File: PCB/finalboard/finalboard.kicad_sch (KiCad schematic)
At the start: 1 part, among them U1 ESP32-S3-WROOM-1

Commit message: FinalBoard Changes
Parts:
- added J1: USB_C_Receptacle_USB2.0, symbol Connector:USB_C_Receptacle_USB2.0
- added J2, J3: Conn_01x04, symbol Connector_Generic:Conn_01x04
- added R1, R2: 5k, symbol Device:R
- added U2: ~, symbol wc_sys_symbol:LCD3.5
- added U3: USBLC6-2SC6, Package_TO_SOT_SMD:SOT-23-6, symbol Power_Protection:USBLC6-2SC6
- added U4: ~, symbol wc_sys_symbol:GPS
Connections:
- net ESP_TX1: now reaches U1.10 (GPIO17/U1TXD/ADC2_CH6)
- net ESP_RX1: now reaches U1.11 (GPIO18/U1RXD/ADC2_CH7/CLK_OUT3)
- net USB_D-: now reaches U1.13 (GPIO19/U1RTS/ADC2_CH8/CLK_OUT2/USB_D-)
- net USB_D-: now also U3.3 (I/O2)
- net USB_D+: now reaches U1.14 (GPIO20/U1CTS/ADC2_CH9/CLK_OUT1/USB_D+)
- net USB_D+: now also U3.1 (I/O1)
- net ESP_RX0: now reaches U1.36 (U0RXD/GPIO44/CLK_OUT2)
- net ESP_TX0: now reaches U1.37 (U0TXD/GPIO43/CLK_OUT1)
- new net: J1.A5 (CC1), R2.1
- new net: J1.A4 (VBUS), J1.A9 (VBUS), J1.B4 (VBUS), J1.B9 (VBUS), U3.5 (VBUS)
- new net: J1.A6 (D+), J1.B6 (D+)
- new net: J1.A7 (D-), J1.B7 (D-)
- new net: J1.B5 (CC2), R1.1
- new net GND: J1.A1 (GND), J1.A12 (GND), J1.B1 (GND), J1.B12 (GND), R1.2, R2.2, U3.2 (GND)
- no-connect marks 0 -> 3
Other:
- company: (none) -> USF IEEE Electrathon
- title: (none) -> Wireless Communication System
- moved on the sheet: U1

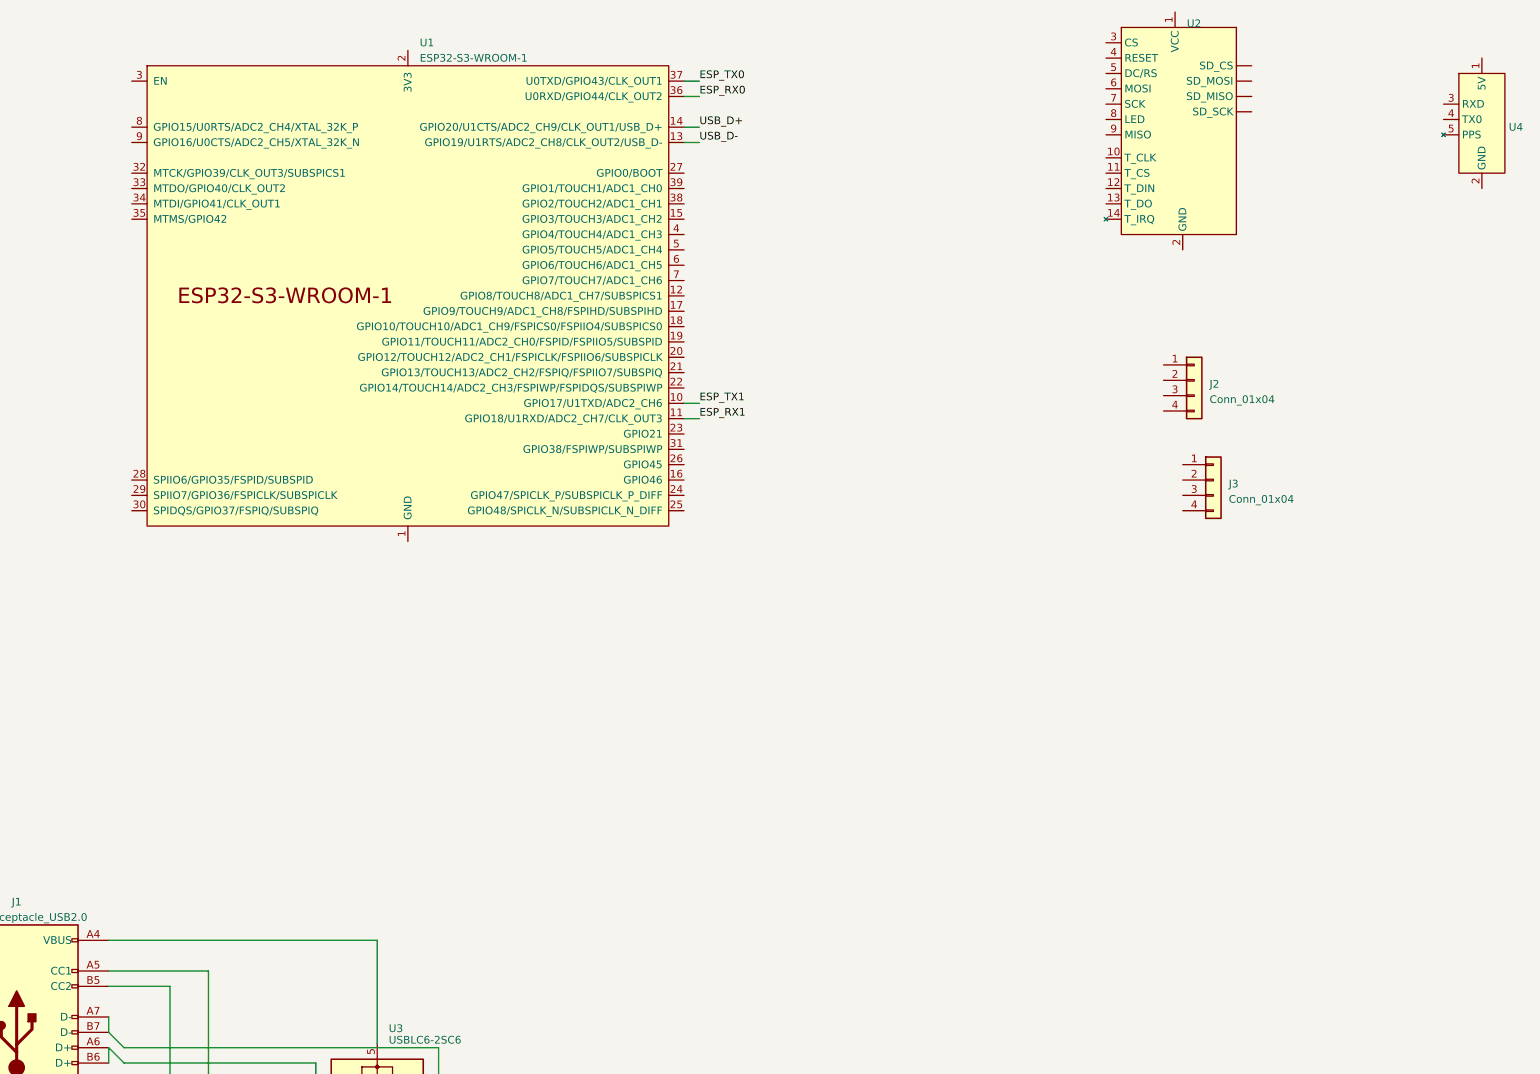
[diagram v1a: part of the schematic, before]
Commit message: Design Iterations
added touch buttons
wired SPI sdcard and display
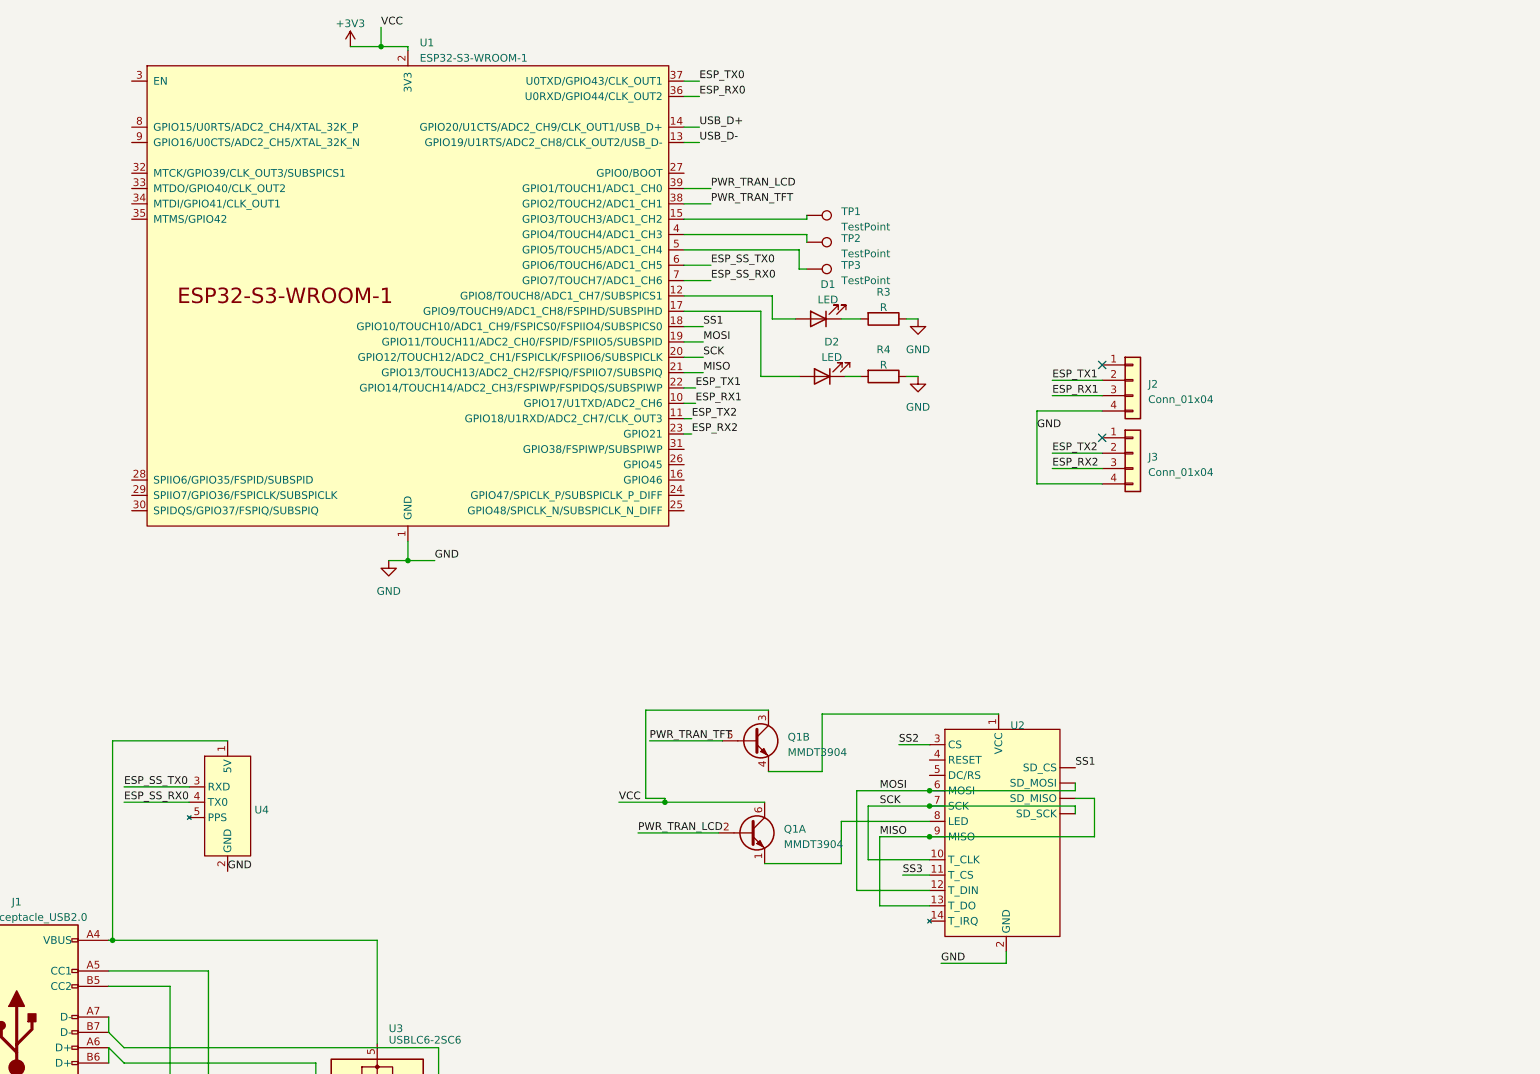
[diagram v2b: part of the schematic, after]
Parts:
- added D1, D2: LED, LED_SMD:LED_2512_6332Metric_Pad1.52x3.35mm_HandSolder, symbol Device:LED
- added Q1: MMDT3904, Package_TO_SOT_SMD:SOT-363_SC-70-6, symbol Transistor_BJT:MMDT3904
- added R3, R4: R, Resistor_SMD:R_1210_3225Metric_Pad1.30x2.65mm_HandSolder, symbol Device:R
- added TP1, TP2, TP3: TestPoint, TestPoint:TestPoint_Pad_D4.0mm, symbol Connector:TestPoint
- J1: footprint (none) -> Connector_USB:USB_C_Receptacle_Palconn_UTC16-G
- J2, J3: footprint (none) -> Connector_PinSocket_2.54mm:PinSocket_1x04_P2.54mm_Vertical_SMD_Pin1Left
- R1, R2: footprint (none) -> Resistor_SMD:R_1210_3225Metric_Pad1.30x2.65mm_HandSolder
- U2: footprint (none) -> wc_sys_footprint:LCD3.5tft
- U4: footprint (none) -> wc_sys_footprint:NEO-6M
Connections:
- net ESP_RX1: now also J2.3 (Pin_3), U1.10 (GPIO17/U1TXD/ADC2_CH6); no longer U1.11 (GPIO18/U1RXD/ADC2_CH7/CLK_OUT3)
- net ESP_TX1: now also J2.2 (Pin_2), U1.22 (GPIO14/TOUCH14/ADC2_CH3/FSPIWP/FSPIDQS/SUBSPIWP); no longer U1.10 (GPIO17/U1TXD/ADC2_CH6)
- net GND: now also J2.4 (Pin_4), J3.4 (Pin_4), U1.1 (GND), U1.40 (GND), U1.41 (GND), U2.2 (GND), U4.2 (GND), R3.1, R4.1
- net at U1.12 (GPIO8/TOUCH8/ADC1_CH7/SUBSPICS1): now also D1.2 (A)
- net at U1.15 (GPIO3/TOUCH3/ADC1_CH2): now also TP1.1
- net at U1.17 (GPIO9/TOUCH9/ADC1_CH8/FSPIHD/SUBSPIHD): now also D2.2 (A)
- net SS1: now reaches U1.18 (GPIO10/TOUCH10/ADC1_CH9/FSPICS0/FSPIIO4/SUBSPICS0)
- net SS1: now also U2. (SD_SCK)
- net MOSI: now reaches U1.19 (GPIO11/TOUCH11/ADC2_CH0/FSPID/FSPIIO5/SUBSPID)
- net MOSI: now also U2. (SD_SCK), U2.12 (T_DIN), U2.6 (MOSI)
- net +3V3: now reaches U1.2 (3V3)
- net +3V3: now also Q1.3 (C2), Q1.6 (C1)
- net SCK: now reaches U1.20 (GPIO12/TOUCH12/ADC2_CH1/FSPICLK/FSPIIO6/SUBSPICLK)
- net SCK: now also U2. (SD_SCK), U2.10 (T_CLK), U2.7 (SCK)
- net MISO: now reaches U1.21 (GPIO13/TOUCH13/ADC2_CH2/FSPIQ/FSPIIO7/SUBSPIQ)
- net MISO: now also U2. (SD_SCK), U2.13 (T_DO), U2.9 (MISO)
- net ESP_RX2: now reaches U1.23 (GPIO21)
- net ESP_RX2: now also J3.3 (Pin_3)
- net PWR_TRAN_TFT: now reaches U1.38 (GPIO2/TOUCH2/ADC1_CH1)
- net PWR_TRAN_TFT: now also Q1.5 (B2)
- net PWR_TRAN_LCD: now reaches U1.39 (GPIO1/TOUCH1/ADC1_CH0)
- net PWR_TRAN_LCD: now also Q1.2 (B1)
- net at U1.4 (GPIO4/TOUCH4/ADC1_CH3): now also TP2.1
- net at U1.5 (GPIO5/TOUCH5/ADC1_CH4): now also TP3.1
- net ESP_SS_TX0: now reaches U1.6 (GPIO6/TOUCH6/ADC1_CH5)
- net ESP_SS_TX0: now also U4.3 (RXD)
- net ESP_SS_RX0: now reaches U1.7 (GPIO7/TOUCH7/ADC1_CH6)
- net ESP_SS_RX0: now also U4.4 (TX0)
- net at U2.1 (VCC): now also Q1.4 (E2)
- net SS3: now reaches U2.11 (T_CS)
- net SS2: now reaches U2.3 (CS)
- net at U2.8 (LED): now also Q1.1 (E1)
- net at J1.A4 (VBUS), J1.A9 (VBUS), J1.B4 (VBUS)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: now also U4.1 (5V)
- net ESP_TX2: now reaches J3.2 (Pin_2)
- net ESP_TX2: now also U1.11 (GPIO18/U1RXD/ADC2_CH7/CLK_OUT3)
- new net: D1.1 (K), R3.2
- new net: D2.1 (K), R4.2
- no-connect marks 3 -> 5
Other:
- moved on the sheet: J2, J3, U2, U4

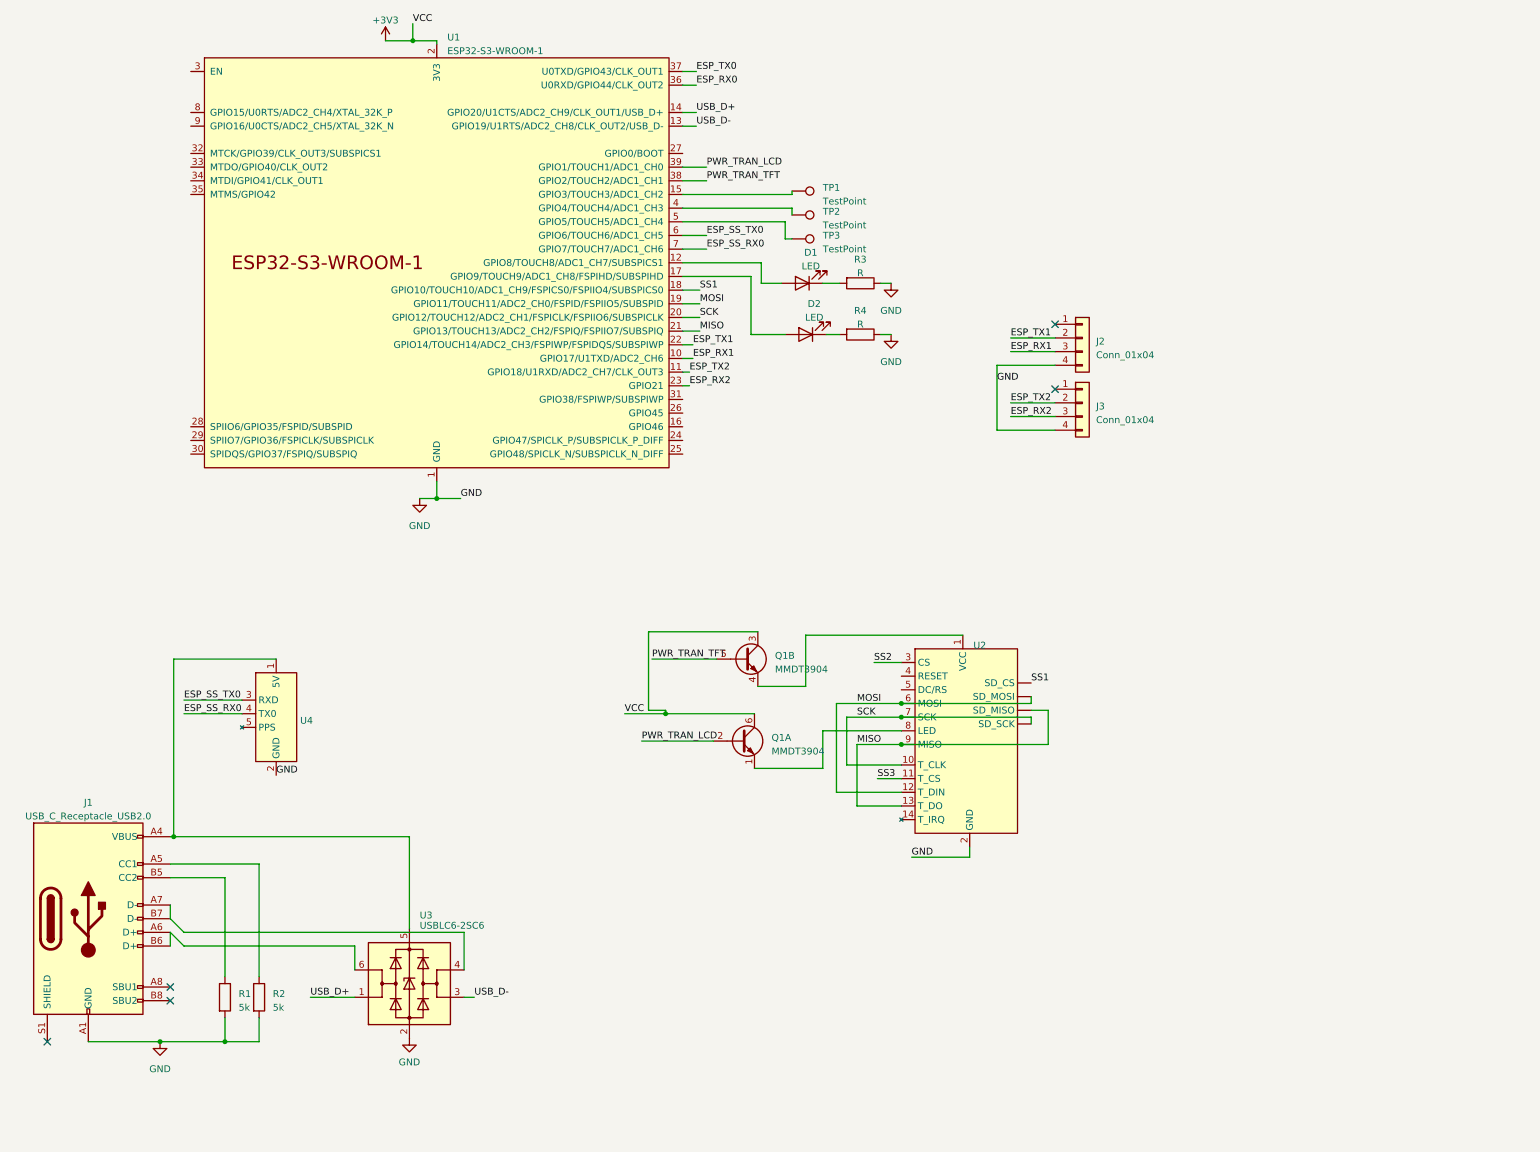
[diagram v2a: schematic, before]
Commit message: Added Components
added lipo charger, regulator, removed type B usb, added 3d Models
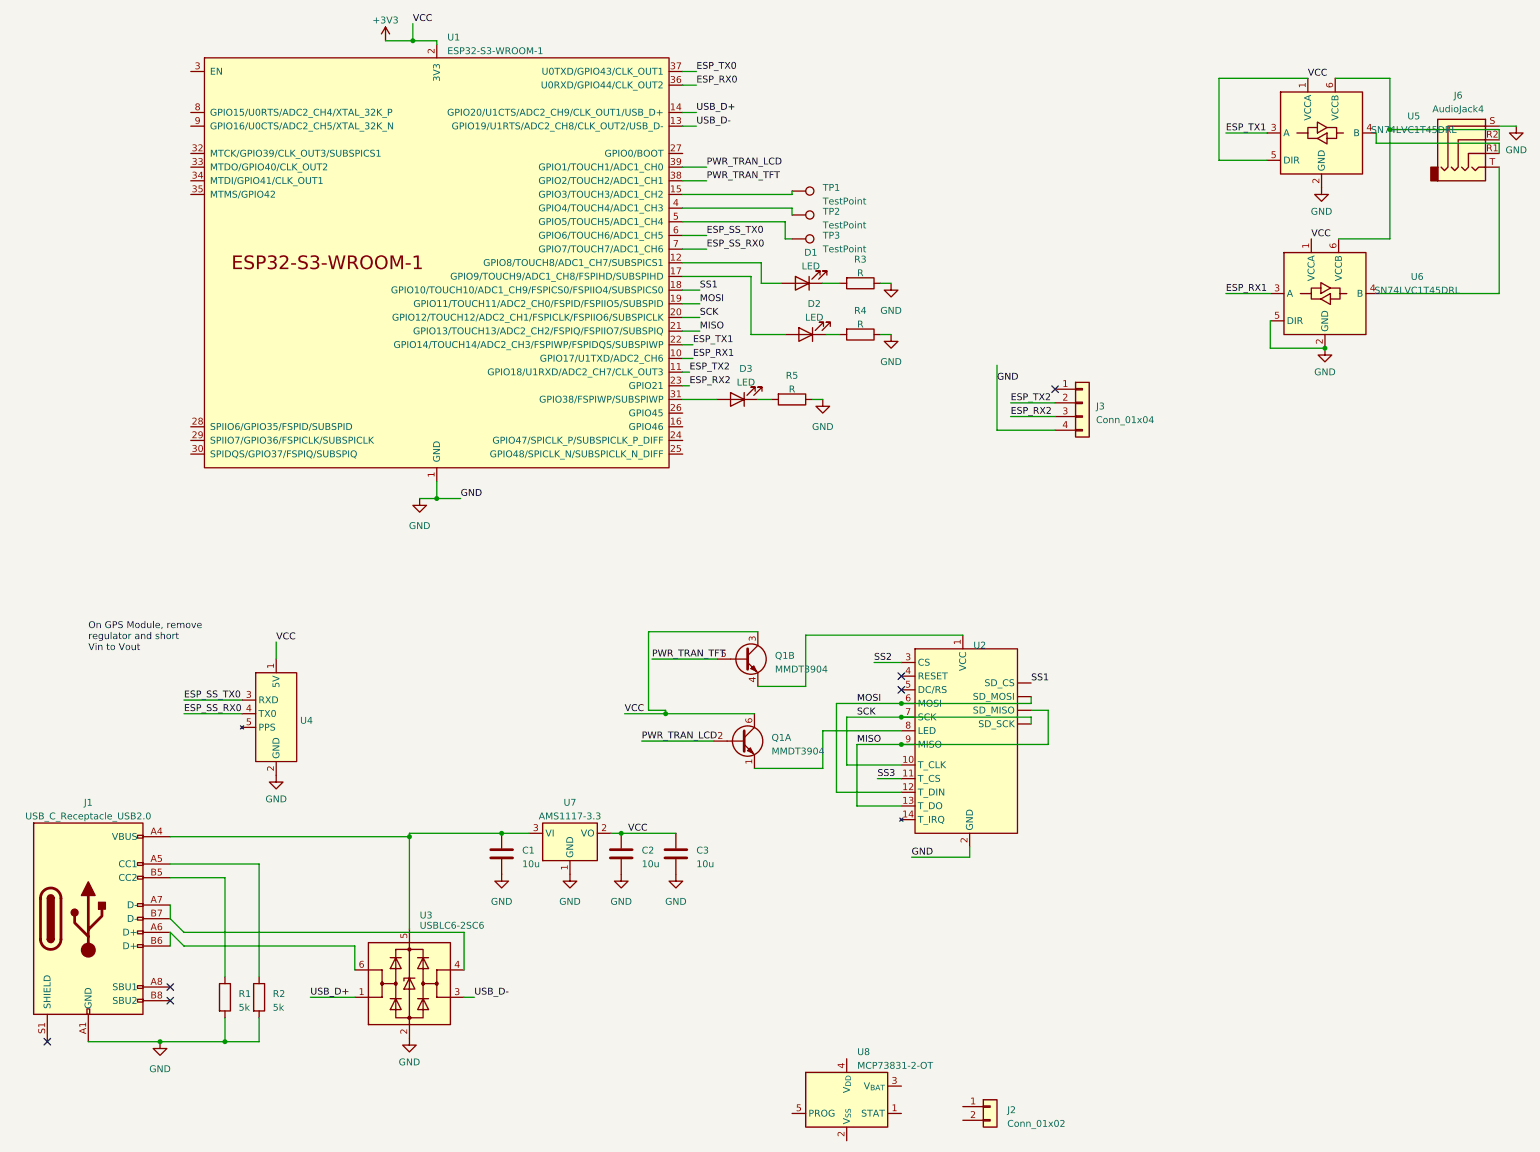
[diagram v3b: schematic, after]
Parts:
- removed J2: Conn_01x04, Connector_PinSocket_2.54mm:PinSocket_1x04_P2.54mm_Vertical_SMD_Pin1Left, symbol Connector_Generic:Conn_01x04
- added C1, C2, C3: 10u, Capacitor_SMD:C_1206_3216Metric, symbol Device:C
- added D3: LED, LED_SMD:LED_1206_3216Metric, symbol Device:LED
- added J2: Conn_01x02, Connector_JST:JST_PH_S2B-PH-K_1x02_P2.00mm_Horizontal, symbol Connector_Generic:Conn_01x02
- added J6: AudioJack4, Connector_Audio:Jack_3.5mm_CUI_SJ2-3593D-SMT_Horizontal, symbol Connector_Audio:AudioJack4
- added R5: R, Resistor_SMD:R_1206_3216Metric, symbol Device:R
- added U5, U6: SN74LVC1T45DRL, Package_TO_SOT_SMD:SOT-563, symbol Logic_LevelTranslator:SN74LVC1T45DRL
- added U7: AMS1117-3.3, Package_TO_SOT_SMD:SOT-223-3_TabPin2, symbol Regulator_Linear:AMS1117-3.3
- added U8: MCP73831-2-OT, Package_TO_SOT_SMD:SOT-23-5, symbol Battery_Management:MCP73831-2-OT
- D1, D2: footprint LED_SMD:LED_2512_6332Metric_Pad1.52x3.35mm_HandSolder -> LED_SMD:LED_1206_3216Metric
- J3: footprint Connector_PinSocket_2.54mm:PinSocket_1x04_P2.54mm_Vertical_SMD_Pin1Left -> Connector_JST:JST_PH_S4B-PH-K_1x04_P2.00mm_Horizontal
- R1, R2, R3, R4: footprint Resistor_SMD:R_1210_3225Metric_Pad1.30x2.65mm_HandSolder -> Resistor_SMD:R_1206_3216Metric
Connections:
- net +3V3: now also U4.1 (5V), C2.1, C3.1, U5.1 (VCCA), U5.5 (DIR), U6.1 (VCCA), U7.2 (VO)
- net ESP_RX1: now also U6.3 (A)
- net ESP_TX1: now also U5.3 (A)
- net GND: now also C1.2, C2.2, C3.2, J6.S, R5.1, U5.2 (GND), U6.2 (GND), U6.5 (DIR), U7.1 (GND)
- net at U1.31 (GPIO38/FSPIWP/SUBSPIWP): now also D3.2 (A)
- net at J1.A4 (VBUS), J1.A9 (VBUS), J1.B4 (VBUS)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: now also C1.1, U7.3 (VI); no longer U4.1 (5V)
- new net: D3.1 (K), R5.2
- new net: J6.R1, U5.4 (B)
- new net: J6.R2, U5.6 (VCCB), U6.6 (VCCB)
- new net: J6.T, U6.4 (B)
- no-connect marks 5 -> 6
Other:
- note added: "On GPS Module, remove regulator and short Vin to Vout"
